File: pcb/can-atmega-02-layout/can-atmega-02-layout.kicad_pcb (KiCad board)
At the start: 2 copper layers, 114 x 98 mm, 180 parts, among them J1 Screw_Terminal_01x02, J2 Screw_Terminal_01x02, J3 Conn_02x03_Odd_Even, J4 Connector_female, U1 LM1117-5.0, U2 TJA1051T, U3 MCP2515-xSO, U4 ATmega328P-A, X1 16MHz, X2 16MHz

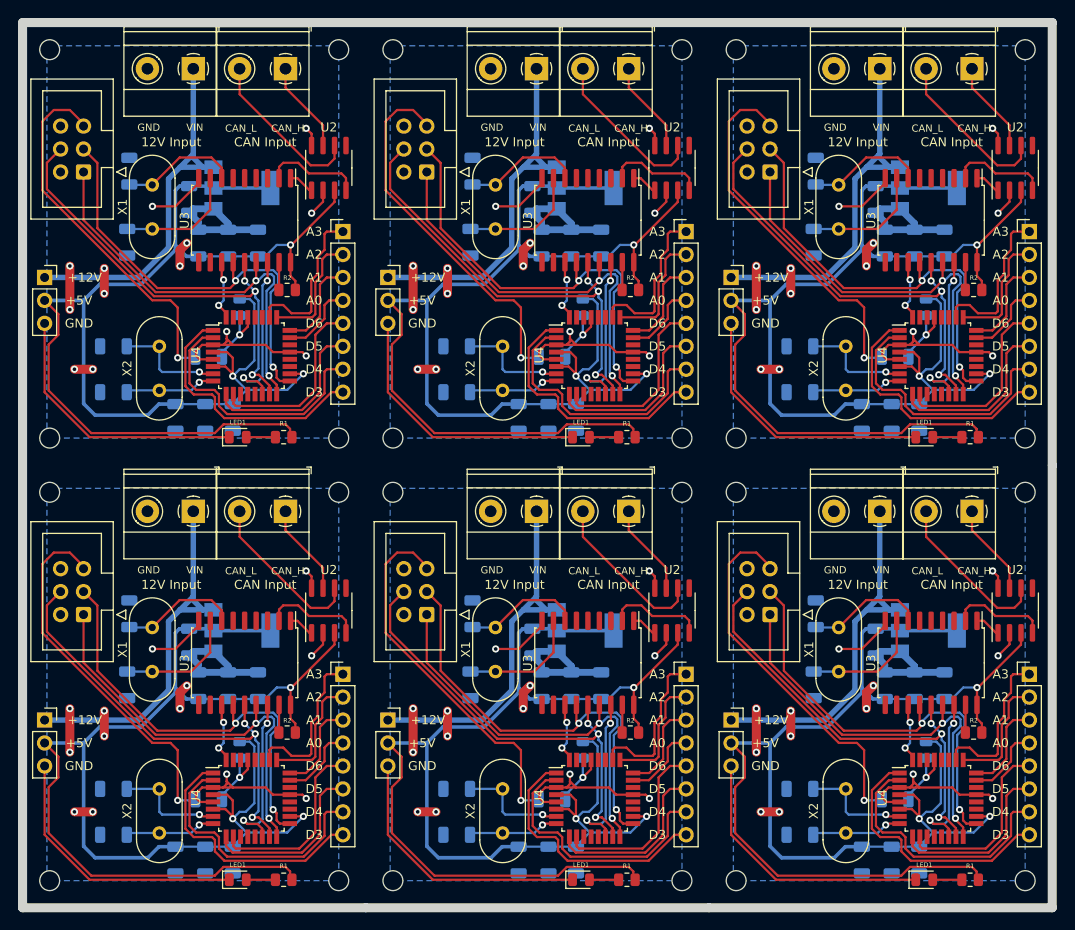
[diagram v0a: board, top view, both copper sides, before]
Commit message: m12 plug; j1939 transition
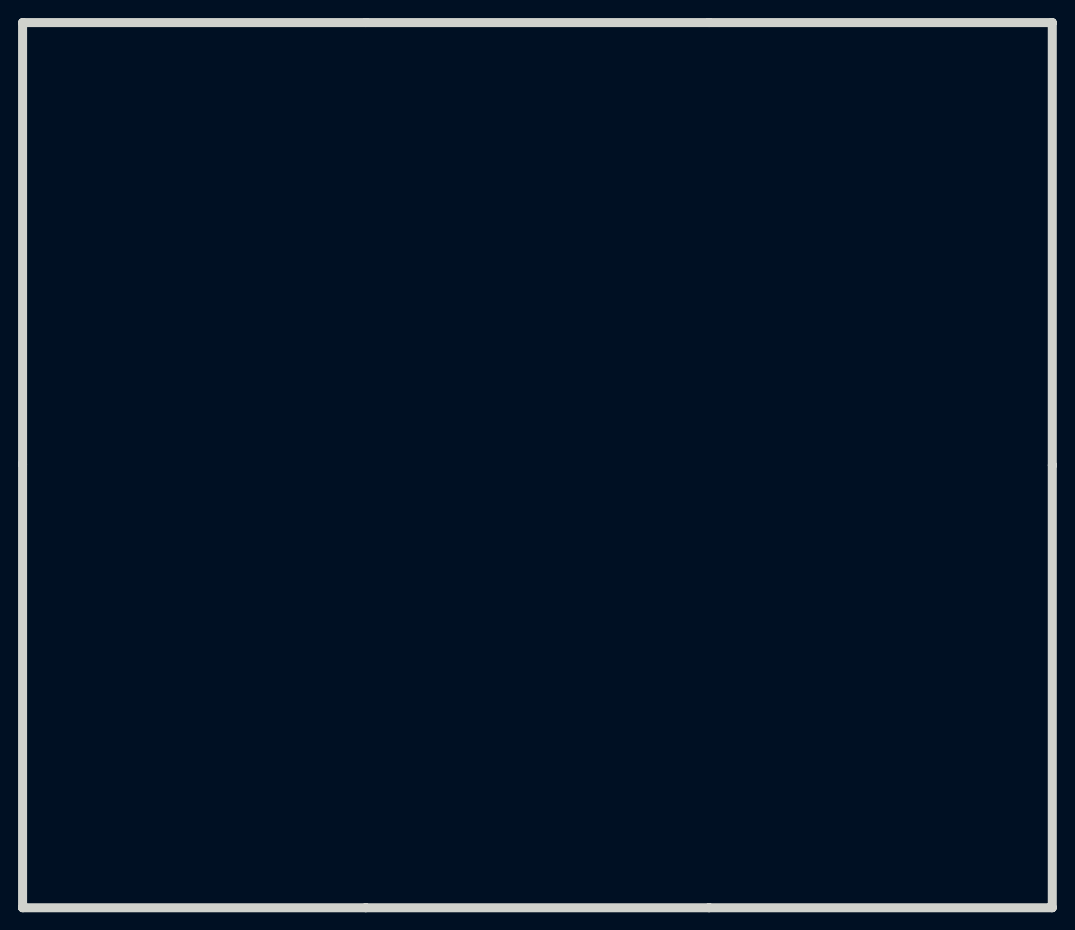
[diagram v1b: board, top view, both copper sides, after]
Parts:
- removed C1 (x6), C12 (x6): 1uF, Capacitor_SMD:C_1206_3216Metric
- removed C10 (x6), C11 (x6), C5 (x6), C6 (x6): 22PF, Capacitor_SMD:C_1206_3216Metric
- removed C2 (x6), C8 (x6): 10uF/16V, Capacitor_SMD:C_1206_3216Metric
- removed C3 (x6), C4 (x6), C7 (x6), C9 (x6): 0.1uF, Capacitor_SMD:C_1206_3216Metric
- removed J1 (x6), J2 (x6): Screw_Terminal_01x02, TerminalBlock_Phoenix:TerminalBlock_Phoenix_MKDS-1,5-2-5.08_1x02_P5.08mm_Horizontal
- removed J3 (x6): Conn_02x03_Odd_Even, Connector_IDC:IDC-Header_2x03_P2.54mm_Vertical
- removed J4 (x6): Connector_female, CAN_ATmega:Connector_female
- removed LED1 (x6): Green, LED_SMD:LED_0805_2012Metric
- removed R1 (x6): 1K, Resistor_SMD:R_0805_2012Metric
- removed R2 (x6), R3 (x6): 10K, Resistor_SMD:R_0805_2012Metric
- removed REF** (x24): MountingHole_2.2mm_M2, MountingHole:MountingHole_2.2mm_M2
- removed U1 (x6): LM1117-5.0, Package_TO_SOT_SMD:SOT-223
- removed U2 (x6): TJA1051T, Package_SO:SOIC-8_3.9x4.9mm_P1.27mm
- removed U3 (x6): MCP2515-xSO, Package_SO:SOIC-18W_7.5x11.6mm_P1.27mm
- removed U4 (x6): ATmega328P-A, Package_QFP:TQFP-32_7x7mm_P0.8mm
- removed X1 (x6), X2 (x6): 16MHz, Crystal:Crystal_HC49-4H_Vertical
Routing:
- net +5V: track 978.1 -> 0.00 mm, vias 18 -> 0
- net GND: track 525.0 -> 0.00 mm, vias 78 -> 0
- net U4_D11_MOSI: track 300.0 -> 0.00 mm, vias 18 -> 0
- net U4_D13_SCK: track 295.2 -> 0.00 mm, vias 12 -> 0
- net U4_D12_MISO: track 279.1 -> 0.00 mm, vias 12 -> 0
- net +12V: track 251.5 -> 0.00 mm
- net U4_RST: track 249.2 -> 0.00 mm, vias 6 -> 0
- net U4_D4: track 176.6 -> 0.00 mm
- net U4_D3: track 173.6 -> 0.00 mm
- net U4_D6: track 123.8 -> 0.00 mm
- net U4_D5: track 118.3 -> 0.00 mm
- net D10_CS: track 112.4 -> 0.00 mm, vias 12 -> 0
- net /CAN_L: track 110.1 -> 0.00 mm
- net U4_A3: track 105.8 -> 0.00 mm
- net /U3_OSC_1: track 81.4 -> 0.00 mm
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- removed copper zone on B.Cu, net GND
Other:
- board text removed: "12V Input"
- board text removed: "CAN Input"
- board text removed: "CAN_H"
- board text removed: "CAN_L"
- board text removed: "GND"
- board text removed: "VIN"
